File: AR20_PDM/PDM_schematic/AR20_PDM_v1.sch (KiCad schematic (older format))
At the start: 0 parts

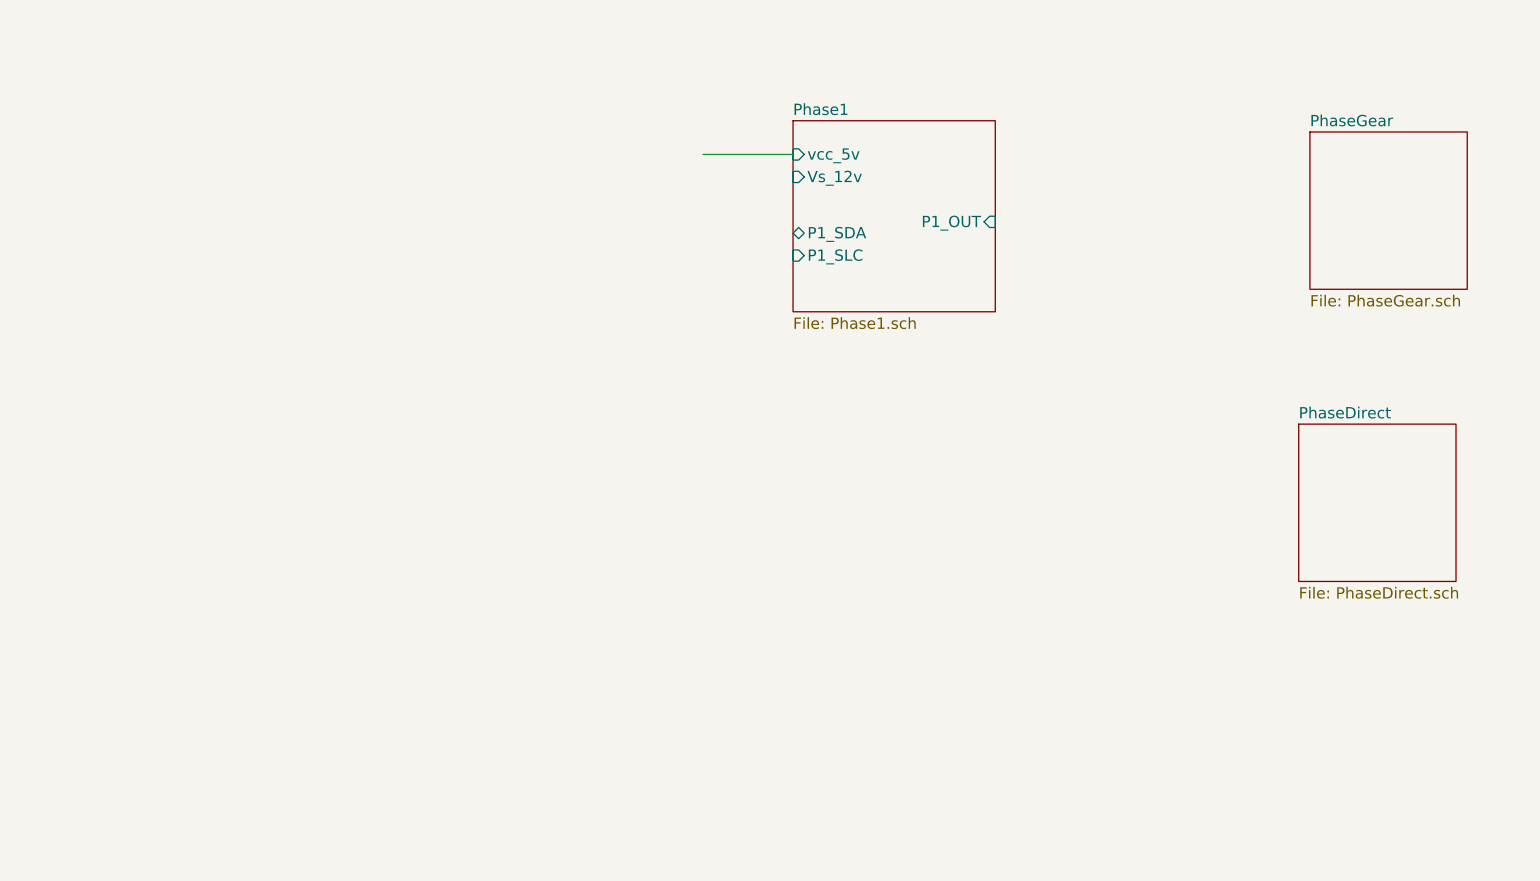
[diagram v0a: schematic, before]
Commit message: Refining pdm schematics
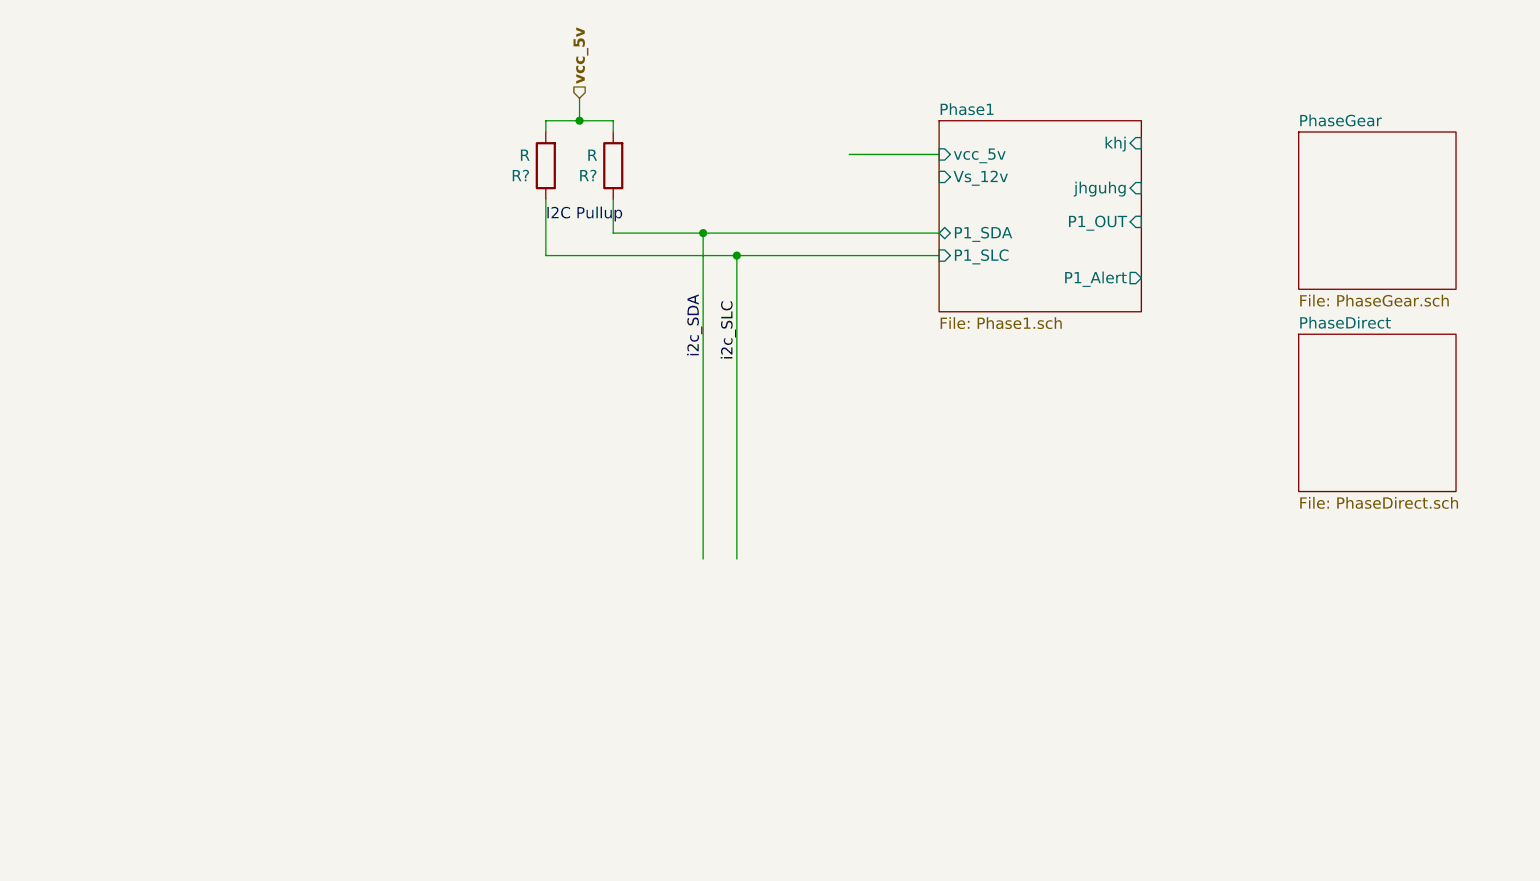
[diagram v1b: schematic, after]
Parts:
- added R? (x2): R, symbol AR20_PDM_v1-rescue:R-Device
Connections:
- net labels added: i2c_SDA, i2c_SLC, vcc_5v
- wire segments 1 -> 14
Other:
- note added: "I2C Pullup"
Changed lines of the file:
@@
 $EndDescr
 Wire Wire Line
-	4800 1300 4400 1300
+	5450 1300 5050 1300
 $Sheet
-S 7050 2500 700  700
+S 7050 2100 700  700
 U 5DA8920B
 F0 "PhaseDirect" 50
@@
 $EndSheet
 $Sheet
-S 7100 1200 700  700
+S 7050 1200 700  700
 U 5DA89204
 F0 "PhaseGear" 50
 F1 "PhaseGear.sch" 50
 $EndSheet
+Wire Wire Line
+	5450 1650 4400 1650
+Wire Wire Line
+	4400 1650 4400 3100
+Wire Wire Line
+	5450 1750 4550 1750
+Wire Wire Line
+	4550 1750 4550 3100
+Text Label 4400 2200 1    50   ~ 0
+i2c_SDA
+Text Label 4550 1950 3    50   ~ 0
+i2c_SLC
+$Comp
+L AR20_PDM_v1-rescue:R-Device R?
+U 1 1 5DAD398E
+P 4000 1350
+AR Path="/5DA89415/5DAD398E" Ref="R?"  Part="1"
+AR Path="/5DAD398E" Ref="R?"  Part="1"
+F 0 "R?" H 4070 1396 50  0000 L CNN
+F 1 "R" H 4070 1305 50  0000 L CNN
+F 2 "" V 3930 1350 50  0001 C CNN
+F 3 "~" H 4000 1350 50  0001 C CNN
+	1    4000 1350
+	-1   0    0    1
+$EndComp
+$Comp
+L AR20_PDM_v1-rescue:R-Device R?
+U 1 1 5DAD3BC1
+P 3700 1350
+AR Path="/5DA89415/5DAD3BC1" Ref="R?"  Part="1"
+AR Path="/5DAD3BC1" Ref="R?"  Part="1"
+F 0 "R?" H 3770 1396 50  0000 L CNN
+F 1 "R" H 3770 1305 50  0000 L CNN
+F 2 "" V 3630 1350 50  0001 C CNN
+F 3 "~" H 3700 1350 50  0001 C CNN
+	1    3700 1350
+	-1   0    0    1
+$EndComp
+Wire Wire Line
+	4400 1650 4000 1650
+Wire Wire Line
+	4000 1500 4000 1650
+Connection ~ 4400 1650
+Wire Wire Line
+	4550 1750 3700 1750
+Wire Wire Line
+	3700 1750 3700 1500
+Connection ~ 4550 1750
+Wire Wire Line
+	4000 1200 4000 1150
+Wire Wire Line
+	4000 1150 3850 1150
+Wire Wire Line
+	3700 1150 3700 1200
+Wire Wire Line
+	3850 1150 3850 1050
+Connection ~ 3850 1150
+Wire Wire Line
+	3850 1150 3700 1150
+Text HLabel 3850 1050 1    50   Input ~ 10
+vcc_5v
+Text Notes 3700 1600 0    50   ~ 0
+I2C Pullup
 $Sheet
-S 4800 1150 900  850
+S 5450 1150 900  850
 U 5DA89415
 F0 "Phase1" 50
 F1 "Phase1.sch" 50
-F2 "Vs_12v" I L 4800 1400 50
-F3 "vcc_5v" I L 4800 1300 50
-F4 "P1_SDA" B L 4800 1650 50
-F5 "P1_SLC" I L 4800 1750 50
-F6 "P1_OUT" I R 5700 1600 50
+F2 "Vs_12v" I L 5450 1400 50
+F3 "vcc_5v" I L 5450 1300 50
+F4 "P1_SDA" B L 5450 1650 50
+F5 "P1_SLC" I L 5450 1750 50
+F6 "P1_OUT" I R 6350 1600 50
+F7 "P1_Alert" O R 6350 1850 50
+F8 "khj" I R 6350 1250 50
+F9 "jhguhg" I R 6350 1450 50
 $EndSheet
 $EndSCHEMATC

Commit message: Refining pdm phase 1
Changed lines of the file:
@@
 I2C Pullup
 $Sheet
-S 5450 1150 900  850
+S 5450 1150 1050 1050
 U 5DA89415
 F0 "Phase1" 50
@@
 F4 "P1_SDA" B L 5450 1650 50
 F5 "P1_SLC" I L 5450 1750 50
-F6 "P1_OUT" I R 6350 1600 50
-F7 "P1_Alert" O R 6350 1850 50
-F8 "khj" I R 6350 1250 50
-F9 "jhguhg" I R 6350 1450 50
+F6 "P1_OUT" I R 6500 1300 50
+F7 "P1_Alert" O L 5450 2050 50
+F8 "P1_EN" I R 6500 1400 50
+F9 "P1_mcu_EN" I R 6500 1500 50
 $EndSheet
 $EndSCHEMATC

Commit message: PDM Phase 1 mostly complete
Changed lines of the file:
@@
 	5450 1300 5050 1300
 $Sheet
-S 7050 2100 700  700
+S 1350 2450 700  700
 U 5DA8920B
 F0 "PhaseDirect" 50
@@
 $EndSheet
 $Sheet
-S 7050 1200 700  700
+S 1350 3650 700  700
 U 5DA89204
 F0 "PhaseGear" 50
